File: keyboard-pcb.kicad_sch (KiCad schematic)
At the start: 29 parts, among them J1 Conn_01x05, J2 USB_C_Receptacle_USB2.0_16P, U1 STM32F072CBTx, U2 74AHCT1G125, U3 XC6206PxxxMR

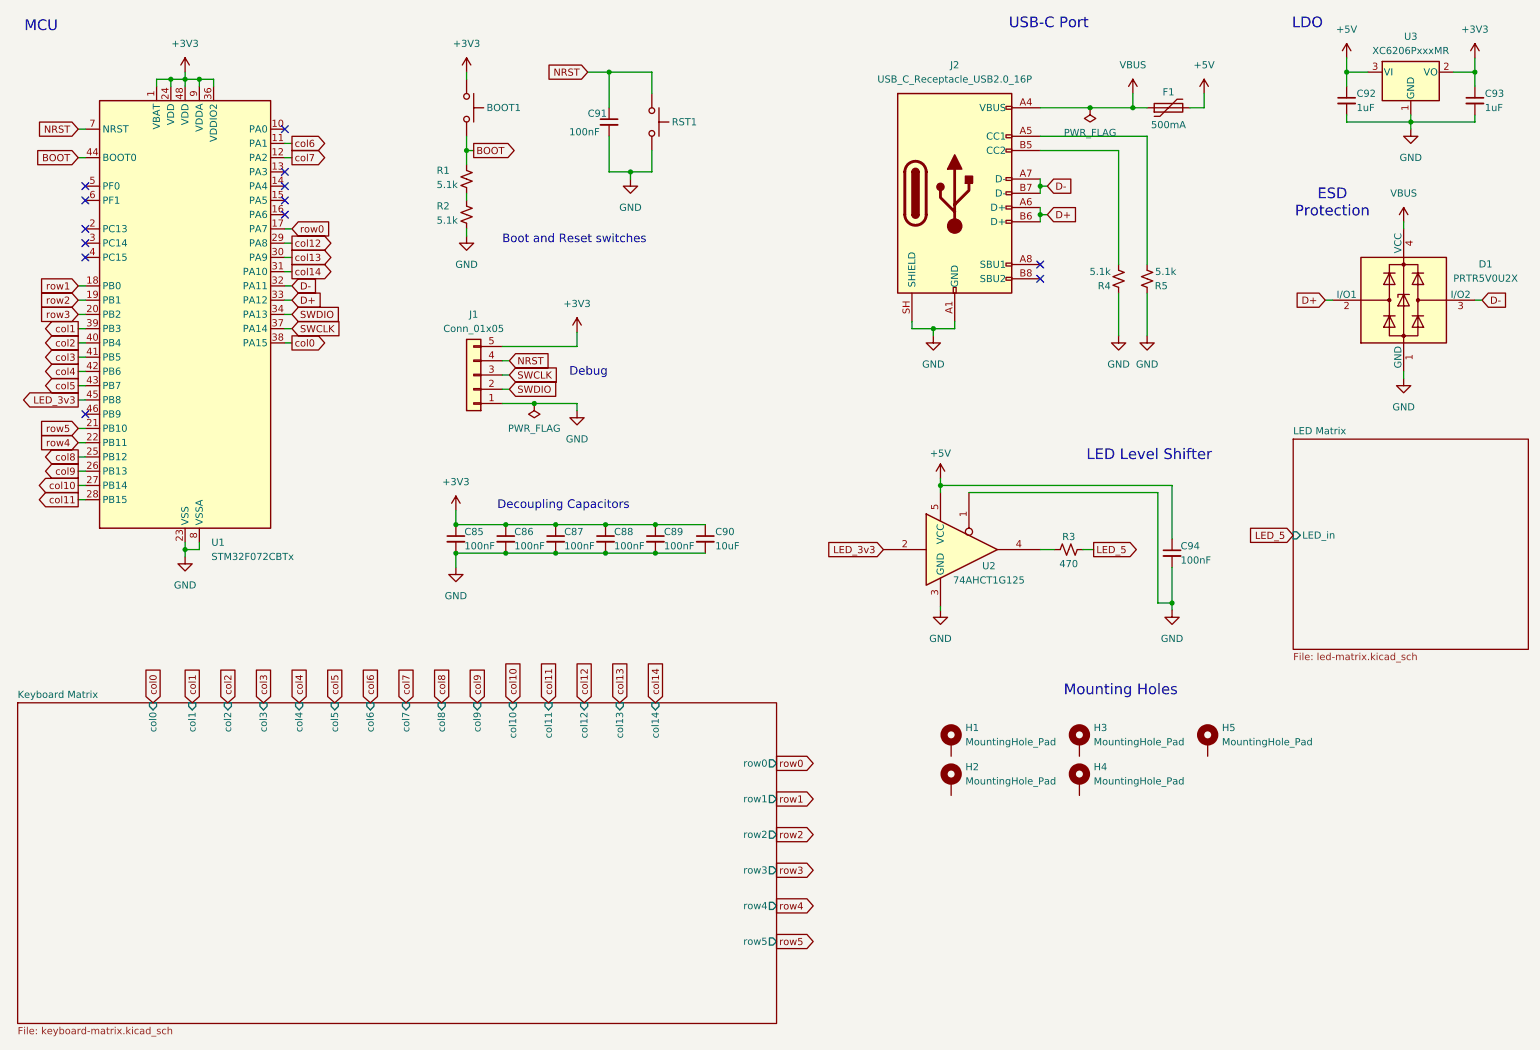
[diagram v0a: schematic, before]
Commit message: revised layout for more compact size
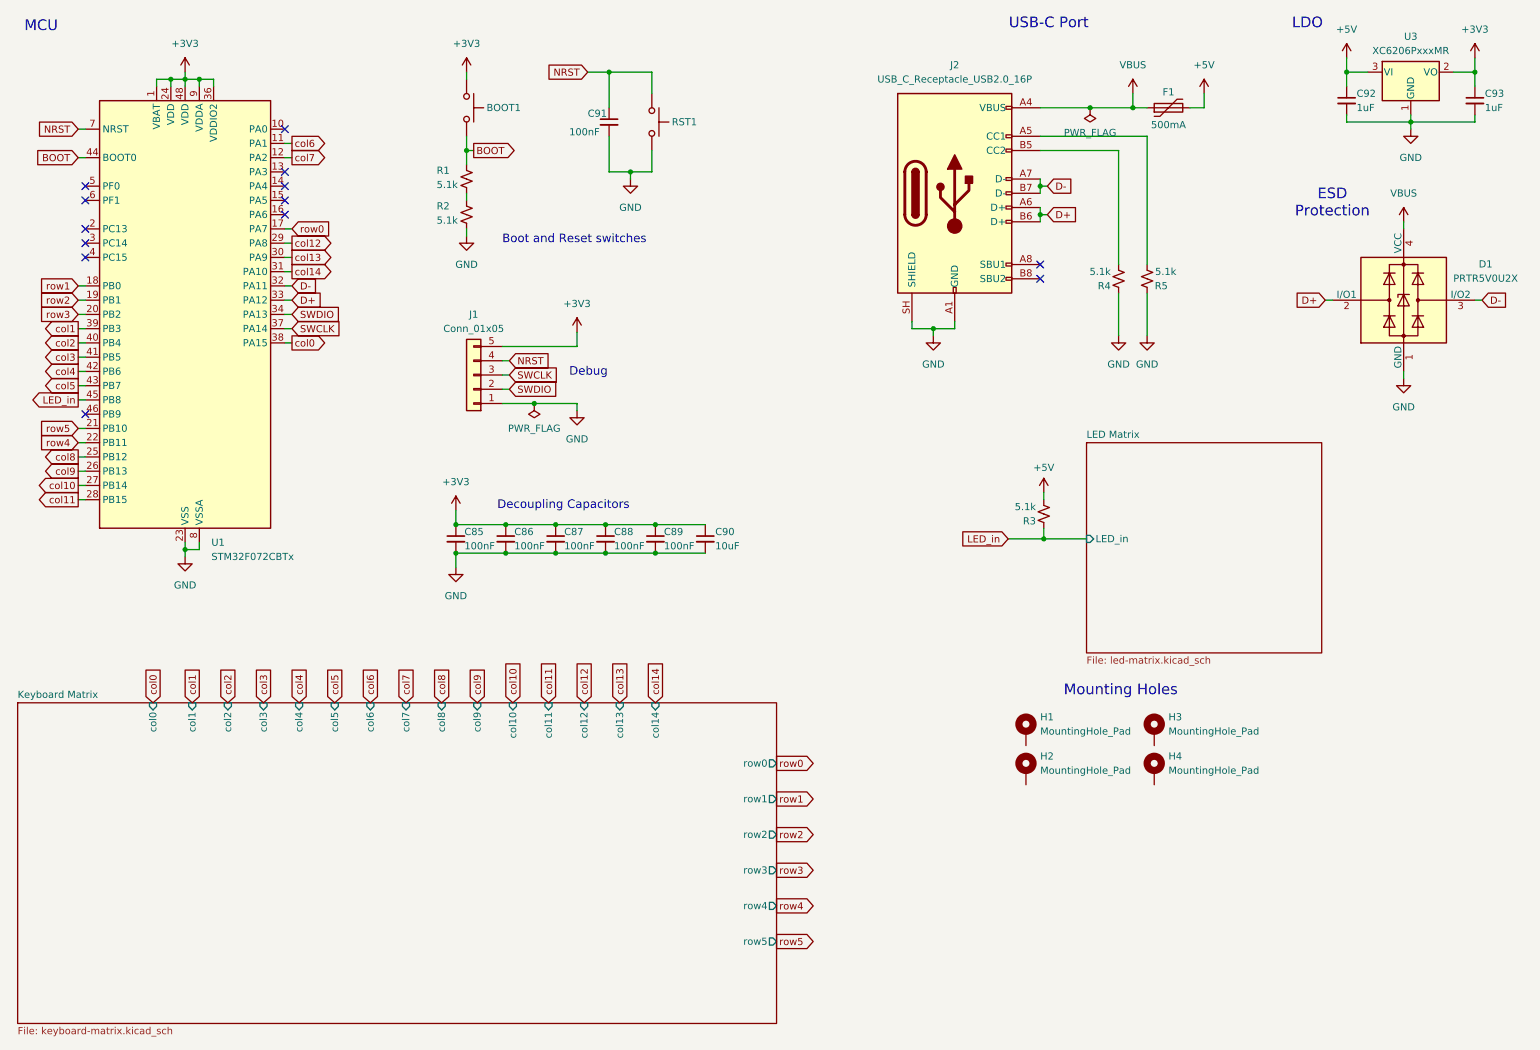
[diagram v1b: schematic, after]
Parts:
- removed C94: 100nF, smd_silkscreen:C_0402_1005Metric, symbol Device:C_Small
- removed H5: MountingHole_Pad, MountingHole:MountingHole_3.2mm_M3_DIN965_Pad, symbol Mechanical:MountingHole_Pad
- removed U2: 74AHCT1G125, Package_TO_SOT_SMD:SOT-23-5, symbol 74xGxx:74AHCT1G125
- R3: value 470 -> 5.1k
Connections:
- net LED_5 is gone; now on net LED_in: R3.2
- net +5V: now also R3.1
- net LED_3v3 renamed LED_in
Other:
- note removed: "LED Level Shifter"
- moved on the sheet: H1, H2, H3, H4

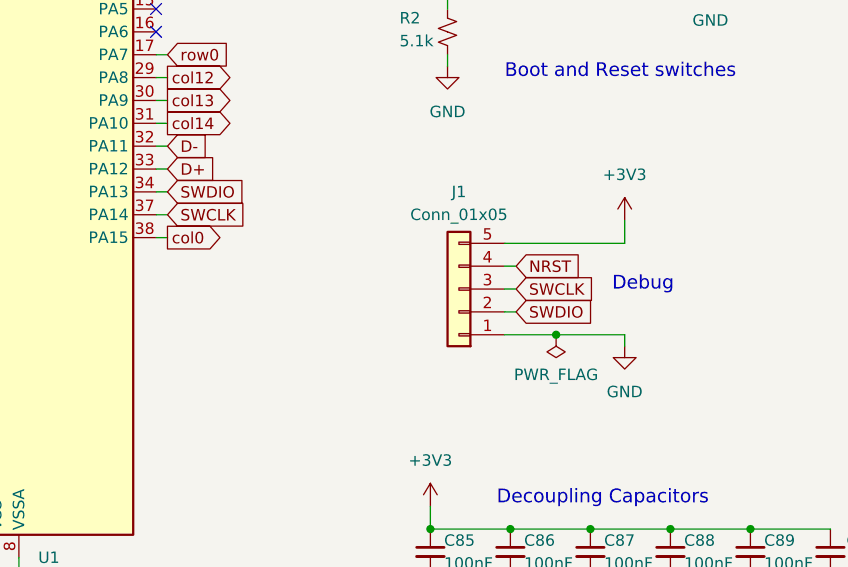
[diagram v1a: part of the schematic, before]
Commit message: updated layout
added 2u stabs for backspace, moved usb and mounting hole for clearance
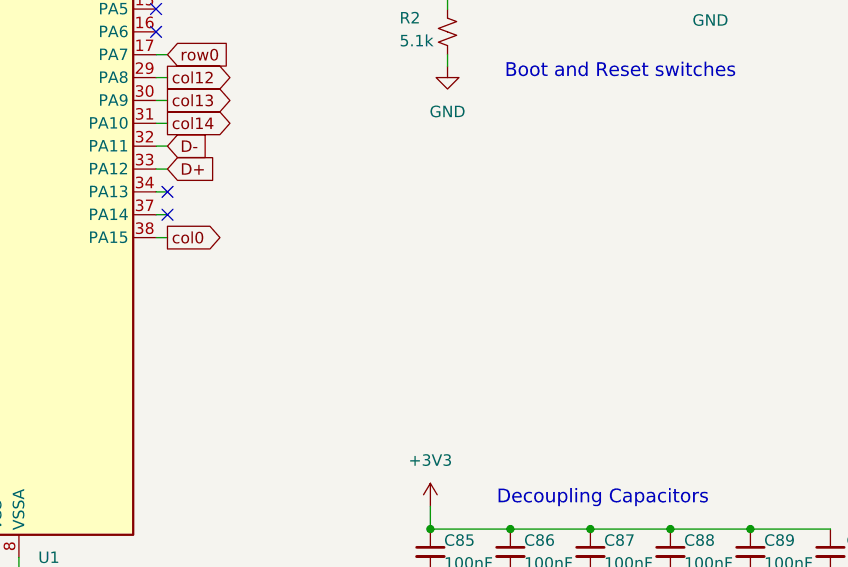
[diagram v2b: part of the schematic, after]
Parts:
- removed J1: Conn_01x05, Connector_PinHeader_2.54mm:PinHeader_1x05_P2.54mm_Vertical, symbol Connector_Generic:Conn_01x05
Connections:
- net SWCLK: no longer names the net of U1.37 (PA14)
- net SWDIO: no longer names the net of U1.34 (PA13)
- no-connect marks 13 -> 15
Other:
- note removed: "Debug"

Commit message: updates
changed fuse rating from 500mA to 1A, added 470 ohm resistor to start of LED data line, added silkscreen art
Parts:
- added R6: 470, smd_silkscreen:R_0402_1005Metric, symbol Device:R_Small_US
- F1: value 500mA -> 1A
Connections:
- net LED_in: now also R6.1
- new net LED Matrix/LED_in: R6.2
- no-connect marks 15 -> 19
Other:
- moved on the sheet: R3
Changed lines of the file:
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@@
 	)
 	(junction
+		(at 193.675 108.585)
+		(diameter 0)
+		(color 0 0 0 0)
+	)
+	(junction
 		(at 100.965 106.045)
 		(diameter 0)
@@
 	)
 	(junction
-		(at 196.85 108.585)
-		(diameter 0)
-		(color 0 0 0 0)
-	)
-	(junction
 		(at 212.725 31.75)
 		(diameter 0)
@@
 	)
 	(no_connect
+		(at 216.535 152.4)
+	)
+	(no_connect
 		(at 196.215 62.23)
 	)
 	(no_connect
+		(at 193.675 145.415)
+	)
+	(no_connect
+		(at 216.535 145.415)
+	)
+	(no_connect
 		(at 26.035 45.72)
 	)
@@
 	)
 	(no_connect
+		(at 193.675 152.4)
+	)
+	(no_connect
 		(at 26.035 55.88)
 	)
@@
 	(wire
 		(pts
-			(xy 196.85 108.585) (xy 204.47 108.585)
+			(xy 193.675 108.585) (xy 196.85 108.585)
 		)
 		(stroke
@@
 	(wire
 		(pts
-			(xy 196.85 106.68) (xy 196.85 108.585)
+			(xy 193.675 105.41) (xy 193.675 108.585)
 		)
 		(stroke
@@
 	(wire
 		(pts
-			(xy 190.5 108.585) (xy 196.85 108.585)
+			(xy 187.325 108.585) (xy 193.675 108.585)
 		)
 		(stroke
@@
 	(wire
 		(pts
-			(xy 196.85 100.33) (xy 196.85 101.6)
+			(xy 193.675 99.06) (xy 193.675 100.33)
+		)
+		(stroke
+			(width 0)
+			(type default)
+		)
+	)
+	(wire
+		(pts
+			(xy 201.93 108.585) (xy 204.47 108.585)
 		)
 		(stroke
@@
 	(global_label "LED_in"
 		(shape input)
-		(at 190.5 108.585 180)
+		(at 187.325 108.585 180)
 		(fields_autoplaced yes)
 		(effects
@@
 		)
 		(property "Intersheetrefs" "${INTERSHEET_REFS}"
-			(at 181.3463 108.585 0)
+			(at 178.1713 108.585 0)
 			(hide yes)
 			(show_name no)
@@
 	)
 	(symbol
+		(lib_id "Device:R_Small_US")
+		(at 199.39 108.585 90)
+		(unit 1)
+		(body_style 1)
+		(exclude_from_sim no)
+		(in_bom yes)
+		(on_board yes)
+		(in_pos_files yes)
+		(dnp no)
+		(property "Reference" "R6"
+			(at 197.866 106.172 90)
+			(show_name no)
+			(do_not_autoplace no)
+			(effects
+				(font
+					(size 1.27 1.27)
+				)
+				(justify right)
+			)
+		)
+		(property "Value" "470"
+			(at 197.358 110.998 90)
+			(show_name no)
+			(do_not_autoplace no)
+			(effects
+				(font
+					(size 1.27 1.27)
+				)
+				(justify right)
+			)
+		)
+		(property "Footprint" "smd_silkscreen:R_0402_1005Metric"
+			(at 199.39 108.585 0)
+			(hide yes)
+			(show_name no)
+			(do_not_autoplace no)
+			(effects
+				(font
+					(size 1.27 1.27)
+				)
+			)
+		)
+		(property "Datasheet" ""
+			(at 199.39 108.585 0)
+			(hide yes)
+			(show_name no)
+			(do_not_autoplace no)
+			(effects
+				(font
+					(size 1.27 1.27)
+				)
+			)
+		)
+		(property "Description" "Resistor, small US symbol"
+			(at 199.39 108.585 0)
+			(hide yes)
+			(show_name no)
+			(do_not_autoplace no)
+			(effects
+				(font
+					(size 1.27 1.27)
+				)
+			)
+		)
+		(pin "2"
+		)
+		(pin "1"
+		)
+		(instances
+			(project "keyboard-pcb"
+				(path "/a41dad29-4328-40a3-b427-6ea31b74fde8"
+					(reference "R6")
+					(unit 1)
+				)
+			)
+		)
+	)
+	(symbol
 		(lib_id "Device:C_Small")
 		(at 119.38 34.29 0)
@@
 			)
 		)
-		(property "Value" "500mA"
+		(property "Value" "1A"
 			(at 219.075 34.798 90)
 			(show_name no)
@@
 			)
 		)
-		(property "Description" "Resettable fuse, polymeric positive temperature coefficient"
+		(property "Description" "https://www.lcsc.com/product-detail/C70082.html"
 			(at 219.075 31.75 0)
 			(hide yes)
@@
 	(symbol
 		(lib_id "power:+5V")
-		(at 196.85 100.33 0)
+		(at 193.675 99.06 0)
 		(unit 1)
 		(body_style 1)
@@
 		(fields_autoplaced yes)
 		(property "Reference" "#PWR011"
-			(at 196.85 104.14 0)
+			(at 193.675 102.87 0)
 			(hide yes)
 			(show_name no)
@@
 		)
 		(property "Value" "+5V"
-			(at 196.85 95.885 0)
+			(at 193.675 94.615 0)
 			(show_name no)
 			(do_not_autoplace no)
@@
 		)
 		(property "Footprint" ""
-			(at 196.85 100.33 0)
+			(at 193.675 99.06 0)
 			(hide yes)
 			(show_name no)
@@
 		)
 		(property "Datasheet" ""
-			(at 196.85 100.33 0)
+			(at 193.675 99.06 0)
 			(hide yes)
 			(show_name no)
@@
 		)
 		(property "Description" "Power symbol creates a global label with name \"+5V\""
-			(at 196.85 100.33 0)
+			(at 193.675 99.06 0)
 			(hide yes)
 			(show_name no)
@@
 	(symbol
 		(lib_id "Device:R_Small_US")
-		(at 196.85 104.14 0)
+		(at 193.675 102.87 0)
 		(unit 1)
 		(body_style 1)
@@
 		(dnp no)
 		(property "Reference" "R3"
-			(at 195.453 105.41 0)
+			(at 192.278 104.14 0)
 			(show_name no)
 			(do_not_autoplace no)
@@
 		)
 		(property "Value" "5.1k"
-			(at 195.453 102.87 0)
+			(at 192.278 101.6 0)
 			(show_name no)
 			(do_not_autoplace no)
@@
 		)
 		(property "Footprint" "smd_silkscreen:R_0402_1005Metric"
-			(at 196.85 104.14 0)
+			(at 193.675 102.87 0)
 			(hide yes)
 			(show_name no)
@@
 		)
 		(property "Datasheet" ""
-			(at 196.85 104.14 0)
+			(at 193.675 102.87 0)
 			(hide yes)
 			(show_name no)
@@
 		)
 		(property "Description" "Resistor, small US symbol"
-			(at 196.85 104.14 0)
+			(at 193.675 102.87 0)
 			(hide yes)
 			(show_name no)
